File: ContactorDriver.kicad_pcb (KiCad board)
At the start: 2 copper layers, 66 x 100 mm, 38 parts, among them J1 PowerConn, J2 DashboardConn, J3 ContactorConn, J4 PrechargeResistorConn, J5 PrechargeResistor, J6 PrechargeResistor, Q1 CSD18511KTT, Q2 PMOS, Q3 CSD18511KTT, U1 RI3-1212S, U2 INA215

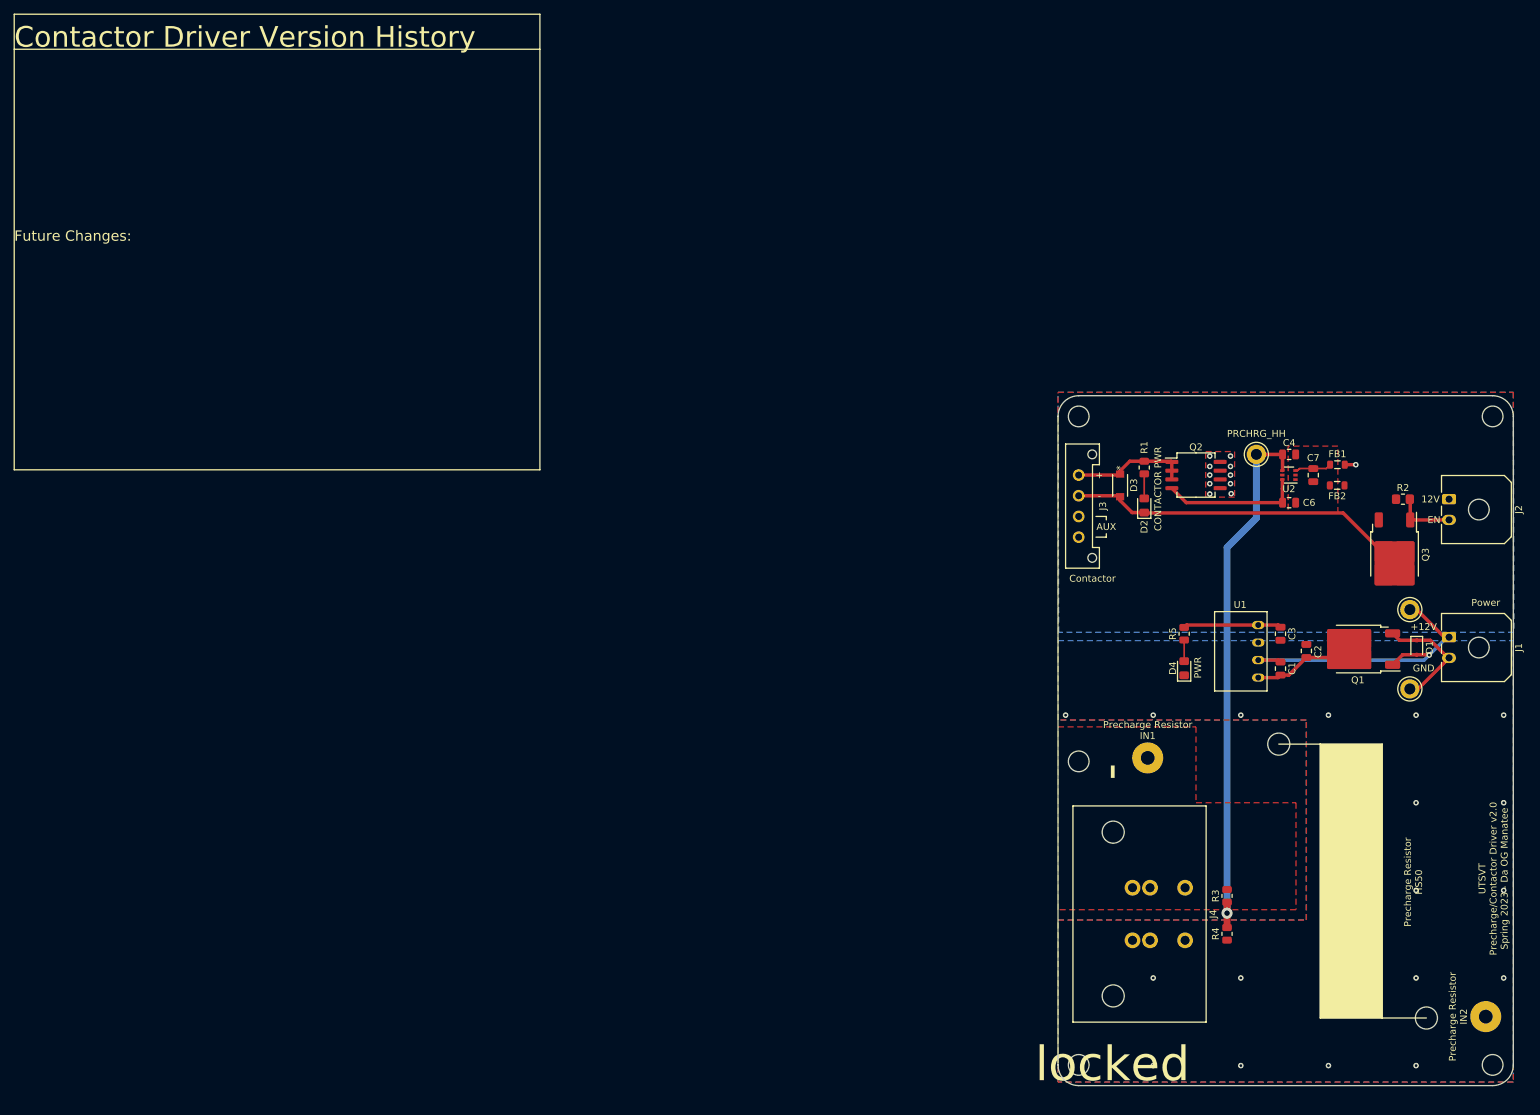
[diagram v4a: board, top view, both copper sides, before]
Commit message: Changed Connector to be molex microfit (#4)
* Changed Connector to be molex microfit

* Addressed Dylan's comments
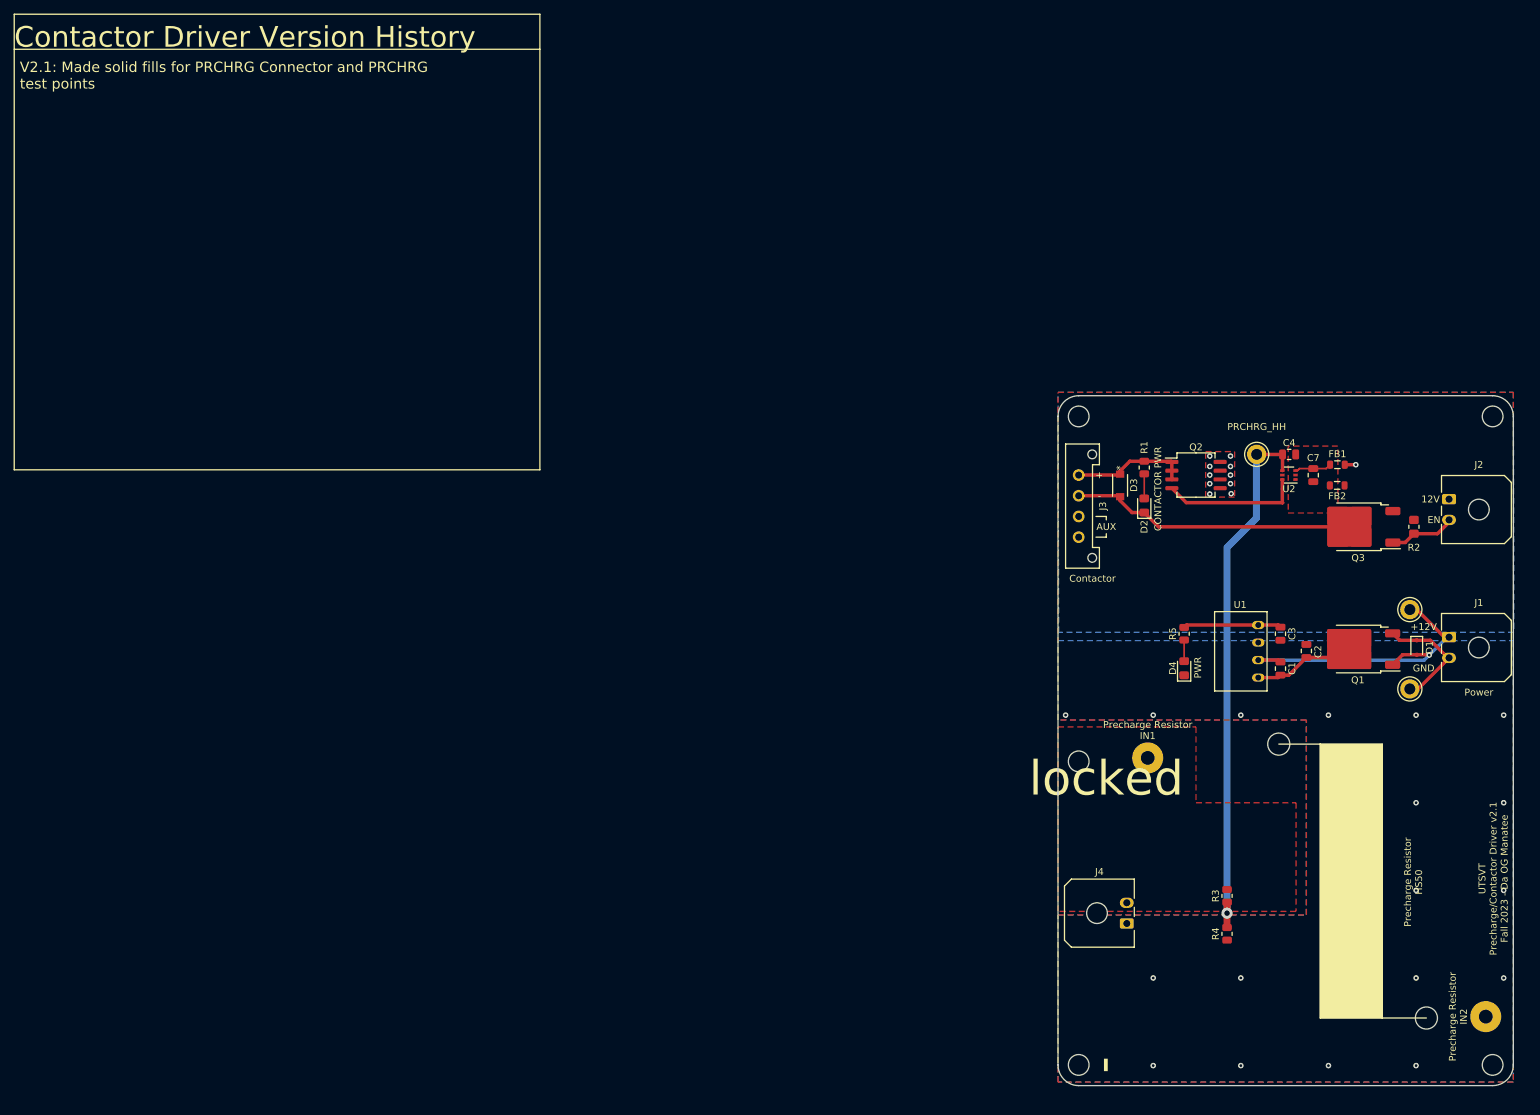
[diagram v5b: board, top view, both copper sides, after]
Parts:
- removed C6: 1u, Capacitor_SMD:C_0805_2012Metric
- C4: value .1u -> 0.01u
- C7: value .1u -> 0.1u
- J4: footprint UTSVT_Connectors:PhoenixContact_PowerCombicon5_GF_2x7.62mm -> Connector_Molex:Molex_Micro-Fit_3.0_43650-0200_1x02_P3.00mm_Horizontal
- U2: value INA215 -> INA213
- moved J4 9.91 mm to (174.0, 144.5), turned to 90 degrees
- moved Q3 6.65 mm to (207.5, 87.0), turned to 180 degrees
- moved R2 4.30 mm to (215.6, 87.0), turned to -90 degrees
- moved PRCHRG_HH 0.05 mm to (192.8, 76.5)
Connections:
- J4 pad 1: Net-(J4-Pin_1) -> GND
- J4 pad 2: GND -> Net-(J4-Pin_2)
- J5 pad 1: Net-(J4-Pin_1) -> Net-(J4-Pin_2)
- R3 pad 2: Net-(J4-Pin_1) -> Net-(J4-Pin_2)
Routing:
- net /CONTACTOR_V-: track 52.4 -> 41.4 mm
- net Net-(J2-Pin_2): track 8.64 -> 9.69 mm
- added copper zone on F.Cu, net Net-(J4-Pin_2)
- removed copper zone on F.Cu, net Net-(J4-Pin_1)
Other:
- board text added: "UTSVT Precharge/Contactor Driver v2.1 Fall 2023 - Da OG Manatee"
- board text added: "V2.1: Made solid fills for PRCHRG Connector and PRCHRG test points"
- board text removed: "Future Changes:"
- board text removed: "UTSVT Precharge/Contactor Driver v2.0 Spring 2023 - Da OG Manatee"

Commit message: Layout completed
Layout attempts to mirror connections on the original V2.1 CDB but in a drastically smaller package.
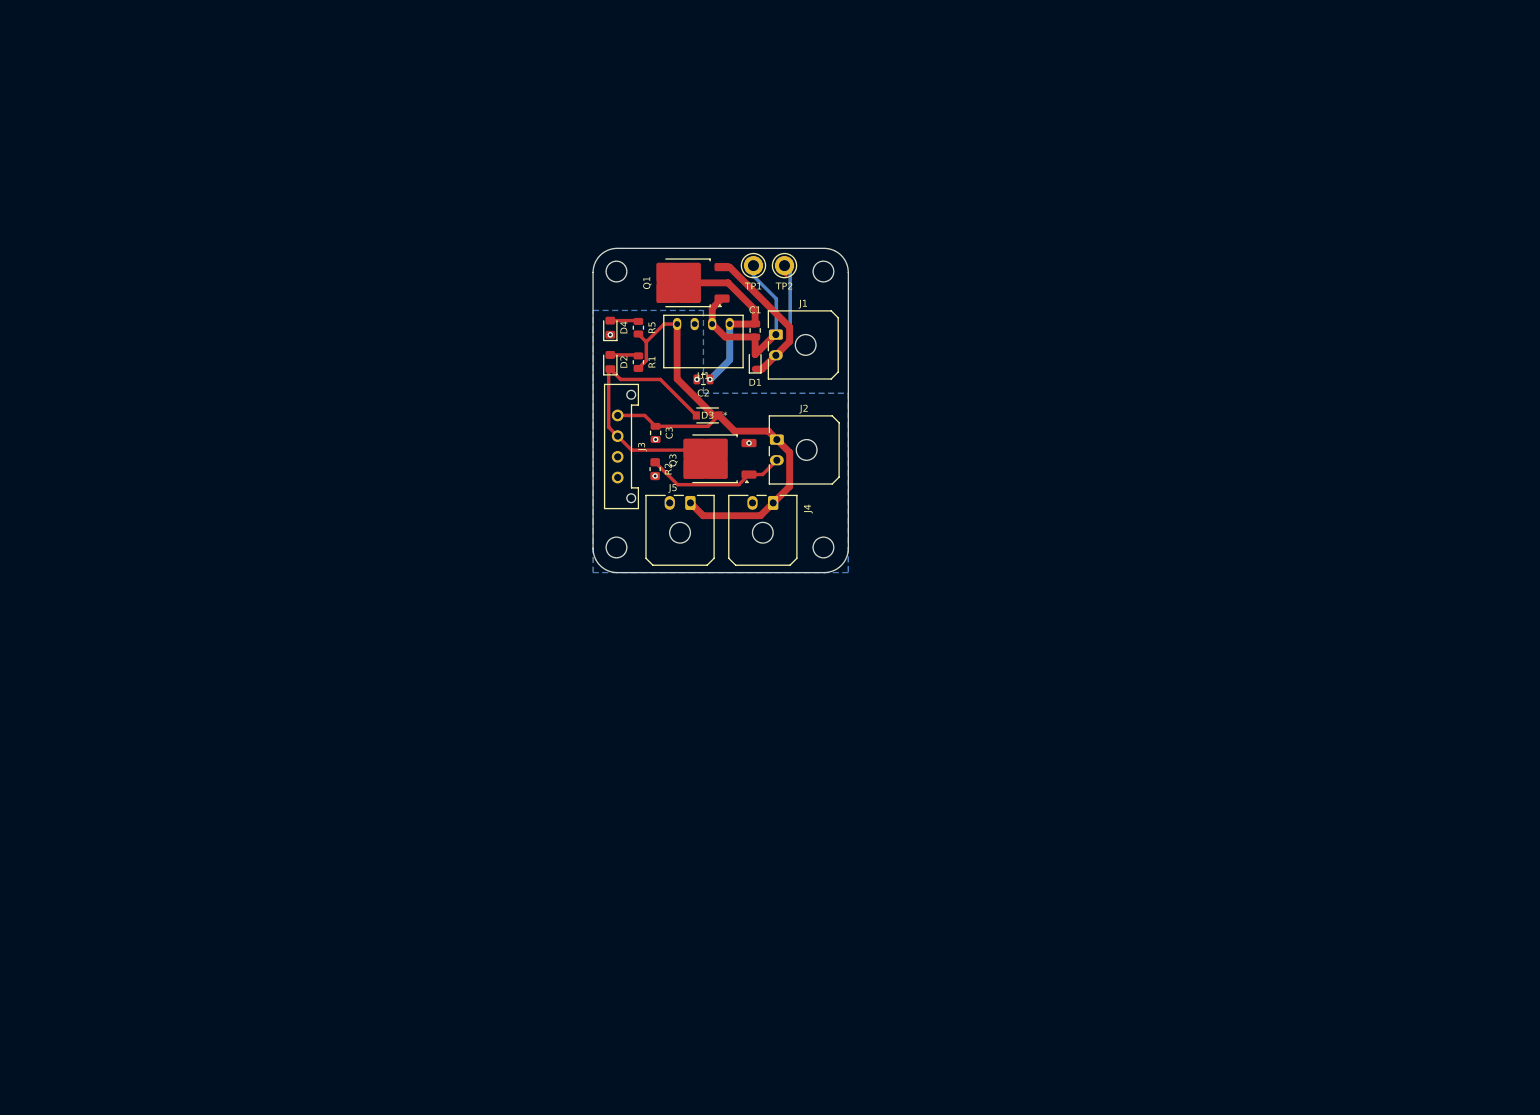
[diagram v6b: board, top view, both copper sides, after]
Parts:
- removed C4: 0.01u, Capacitor_SMD:C_0805_2012Metric
- removed C7: 0.1u, Capacitor_SMD:C_0805_2012Metric
- removed FB1, FB2: FerriteBead_Small, Inductor_SMD:L_0805_2012Metric
- removed H5, H6, H7: M3, MountingHole:MountingHole_3mm
- removed J6: PrechargeResistor, Connector_Wire:SolderWirePad_1x01_Drill2mm
- removed PRCHRG_HH: PRCHRG_HH, TestPoint:TestPoint_Keystone_5005-5009_Compact
- removed Q2: PMOS, Package_SO:SO-8_5.3x6.2mm_P1.27mm
- removed R3: 100k, Resistor_SMD:R_0805_2012Metric
- removed R4: 2.2k, Resistor_SMD:R_0805_2012Metric
- removed U2: INA213, Package_TO_SOT_SMD:SOT-363_SC-70-6
- H1, H2: value M4 -> M3; footprint MountingHole:MountingHole_3.2mm_M3 -> MountingHole:MountingHole_3mm
- J4: value PrechargeResistorConn -> FanConn1
- J5: value PrechargeResistor -> FanConn2; footprint Connector_Wire:SolderWirePad_1x01_Drill2mm -> Connector_Molex:Molex_Micro-Fit_3.0_43650-0200_1x02_P3.00mm_Horizontal
- moved H2 159.7 mm to (100.0, 50.0), turned to 0 degrees
- moved H3 122.6 mm to (130.0, 90.0)
- moved Q1 110.7 mm to (110.3, 51.6)
- moved R2 110.3 mm to (105.6, 78.6), turned to 90 degrees
- moved TP2 109.5 mm to (124.4, 49.1), turned to 180 degrees
- moved TP1 107.4 mm to (119.9, 49.1), turned to 180 degrees
- moved J1 107.0 mm to (123.1, 59.1)
- moved D1 104.5 mm to (120.1, 63.1), turned to 90 degrees
- moved H4 100.6 mm to (100.0, 90.0)
- moved J2 97.8 mm to (123.2, 74.4)
- moved D4 96.7 mm to (99.1, 58.1)
- moved C2 95.8 mm to (112.6, 65.6), turned to 180 degrees
- moved C3 95.1 mm to (105.7, 73.4)
- moved H1 95.1 mm to (130.0, 50.0), turned to 0 degrees
- moved Q3 93.8 mm to (114.2, 77.1)
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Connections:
- D3 pad 1: /CONTACTOR_V+ -> +12V
- J3 pad 1: /CONTACTOR_V+ -> +12V
- J4 pad 1: GND -> +12V
- J4 pad 2: Net-(J4-Pin_2) -> GND
- J5 pad 1: Net-(J4-Pin_2) -> +12V
- R1 pad 2: /CONTACTOR_V+ -> +12V
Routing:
- net /PRCHRG_HH: track 78.1 -> 0.00 mm, vias 1 -> 0
- net +12V: track 16.4 -> 78.0 mm, vias 11 -> 0
- net Net-(D1-A1): track 17.2 -> 37.8 mm
- net /EN_CURR: track 20.3 -> 0.00 mm
- net /CONTACTOR_V+: track 17.2 -> 0.00 mm
- net Net-(D1-A2): track 45.6 -> 29.5 mm, vias 1 -> 0
- net Net-(Q1-D): track 12.8 -> 27.7 mm, vias 0 -> 1
- net Net-(J2-Pin_2): track 9.69 -> 20.4 mm
- net Net-(U2-V+): track 5.37 -> 0.00 mm
- net /CONTACTOR_V-: track 41.4 -> 38.1 mm
- net Net-(D4-A): track 3.06 -> 4.28 mm
- net Net-(D2-A): track 3.56 -> 4.32 mm
- net GND: vias 21 -> 5
- removed copper zone on B.Cu, net +12V
- removed copper zone on F.Cu, net +12V
- removed copper zone on F.Cu, net GND
- removed copper zone on F.Cu, net Net-(J4-Pin_2)
- removed copper zone on F.Cu, net Net-(U2-REF)
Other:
- board size 66 x 100 mm -> 37 x 47 mm
- board text removed: "+"
- board text removed: "+12V"
- board text removed: "-"
- board text removed: "12V"
- board text removed: "44mm"
- board text removed: "50mm"
- board text removed: "60mm"
- board text removed: "AUX"
- board text removed: "CONTACTOR PWR"
- board text removed: "Contactor"
- board text removed: "Contactor Driver Version History"
- board text removed: "Dr. Gary Hallock"
- board text removed: "EN"
- board text removed: "GND"
- board text removed: "M3"
- board text removed: "PWR"
- board text removed: "Power"
- board text removed: "Precharge Resistor HS50"
- board text removed: "Precharge Resistor IN1"
- board text removed: "Precharge Resistor IN2"
- board text removed: "UTSVT Precharge/Contactor Driver v2.1 Fall 2023 - Da OG Manatee"
- board text removed: "V2.1: Made solid fills for PRCHRG Connector and PRCHRG test points"
- board text removed: "locked"

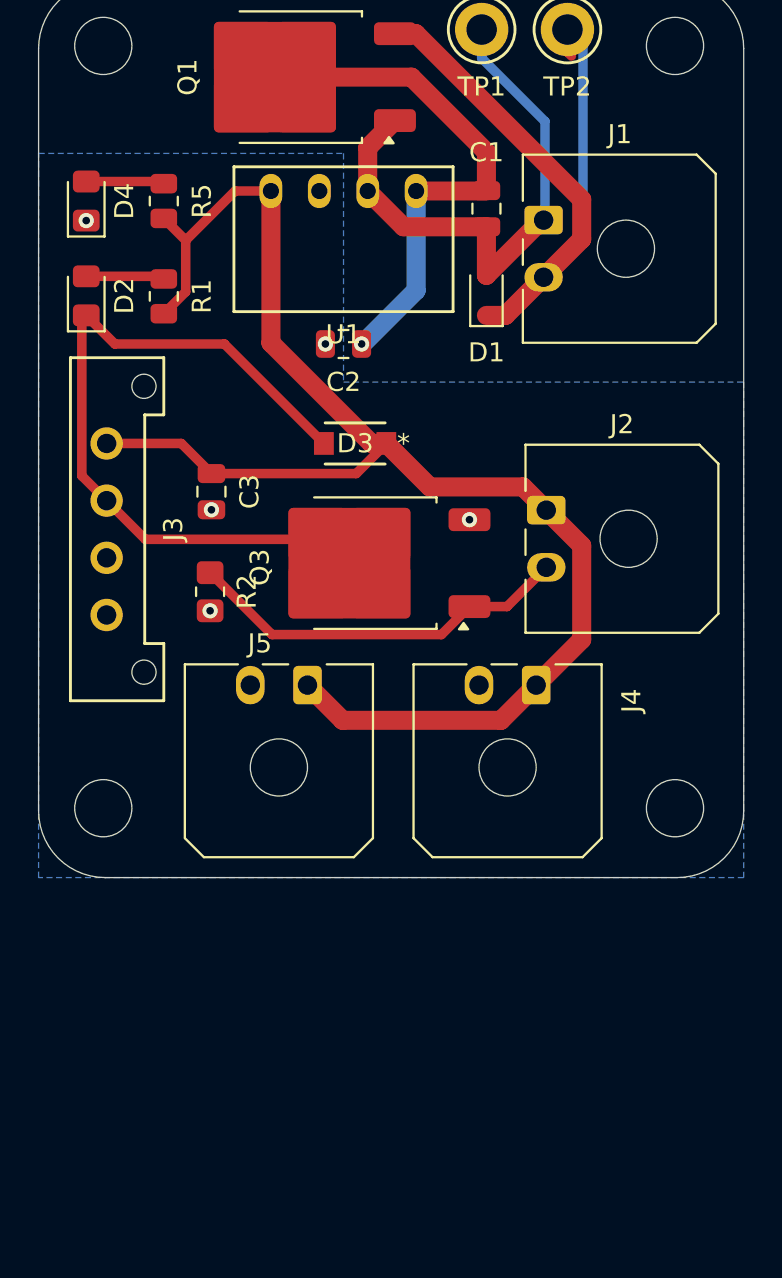
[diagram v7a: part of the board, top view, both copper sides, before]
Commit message: Layout Updated
Updated layout to match updated schematic.
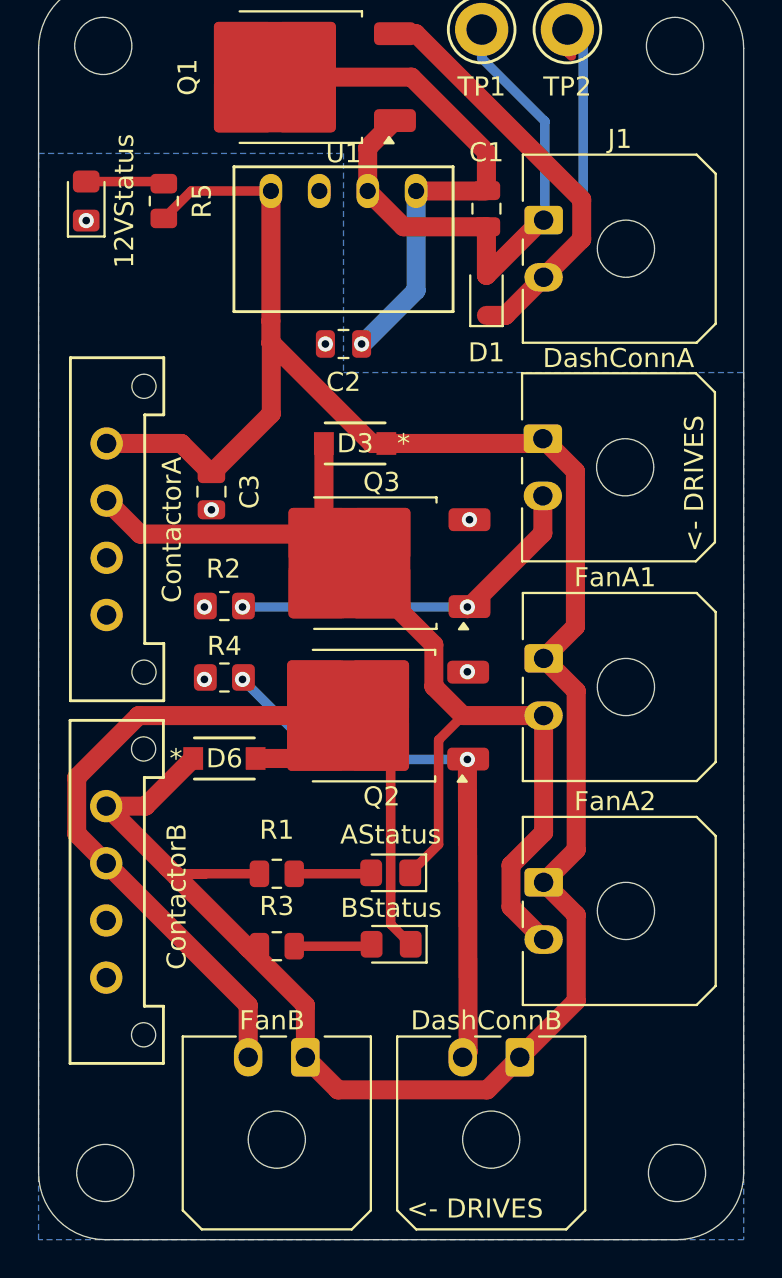
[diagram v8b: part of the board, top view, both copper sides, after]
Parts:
- added BStatus: Green, LED_SMD:LED_0805_2012Metric_Pad1.15x1.40mm_HandSolder, F.Cu at (115.1, 97.1)
- added ContactorB: ContactorBConn, UTSVT_Connectors:Molex_MicroFit3.0_1x4xP3.00mm_PolarizingPeg_Vertical, F.Cu at (100.2, 89.9)
- added D6: V2F22HM3/H, UTSVT_Passive:V2F22HM, F.Cu at (106.4, 87.4)
- added DashConnB: DashboardConnB, Connector_Molex:Molex_Micro-Fit_3.0_43650-0200_1x02_P3.00mm_Horizontal, F.Cu at (121.9, 103.1)
- added FanB: FanConn3, Connector_Molex:Molex_Micro-Fit_3.0_43650-0200_1x02_P3.00mm_Horizontal, F.Cu at (110.6, 103.1)
- added Q2: CSD18511KTT, Package_TO_SOT_SMD:TO-252-2, F.Cu at (114.1, 85.1)
- added R3: 10k, Resistor_SMD:R_0805_2012Metric, F.Cu at (109.1, 97.2)
- added R4: 100k, Resistor_SMD:R_0805_2012Metric_Pad1.20x1.40mm_HandSolder, F.Cu at (106.4, 83.1)
- ContactorA: renamed from J3; value ContactorConn -> ContactorAConn
- DashConnA: renamed from J2; value DashboardConn -> DashboardConnA
- moved AStatus 34.2 mm to (115.1, 93.4), turned to 180 degrees
- moved R1 30.9 mm to (109.1, 93.4), turned to 180 degrees
- moved H3 19.1 mm to (130.1, 109.1)
- moved H4 19.1 mm to (100.1, 109.1)
- moved FanA2 16.1 mm to (123.1, 93.9), turned to -90 degrees
- moved DashConnA 3.75 mm to (123.1, 70.6)
- moved FanA1 1.45 mm to (123.1, 82.1), turned to -90 degrees
- moved R2 1.06 mm to (106.4, 79.4), turned to 0 degrees
- renumbered D4 to 12VStatus, D2 to AStatus, J4 to FanA1, J5 to FanA2
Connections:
- AStatus pad 1: /CONTACTOR_V- -> /CONTACTOR_A_V-
- ContactorA pad 2: /CONTACTOR_V- -> /CONTACTOR_A_V-
- D3 pad 2: /CONTACTOR_V- -> /CONTACTOR_A_V-
- FanA1 pad 2: GND -> /CONTACTOR_A_V-
- FanA2 pad 2: GND -> /CONTACTOR_A_V-
- Q3 pad 2: /CONTACTOR_V- -> /CONTACTOR_A_V-
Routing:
- net /CONTACTOR_A_V-: track 0.00 -> 54.0 mm
- net +12V: track 78.0 -> 126.8 mm
- net /CONTACTOR_B_V-: track 0.00 -> 48.6 mm
- net /CONTACTOR_V-: track 38.1 -> 0.00 mm
- net Net-(J6-Pin_2): track 0.00 -> 29.3 mm, vias 0 -> 2
- net Net-(BStatus1-A): track 0.00 -> 4.25 mm
- net Net-(J2-Pin_2): track 20.4 -> 19.6 mm, vias 0 -> 2
- net GND: vias 5 -> 7
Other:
- board size 37 x 47 mm -> 37 x 66 mm
- board text added: "<- DRIVES"
